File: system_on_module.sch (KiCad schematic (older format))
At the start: 1 part

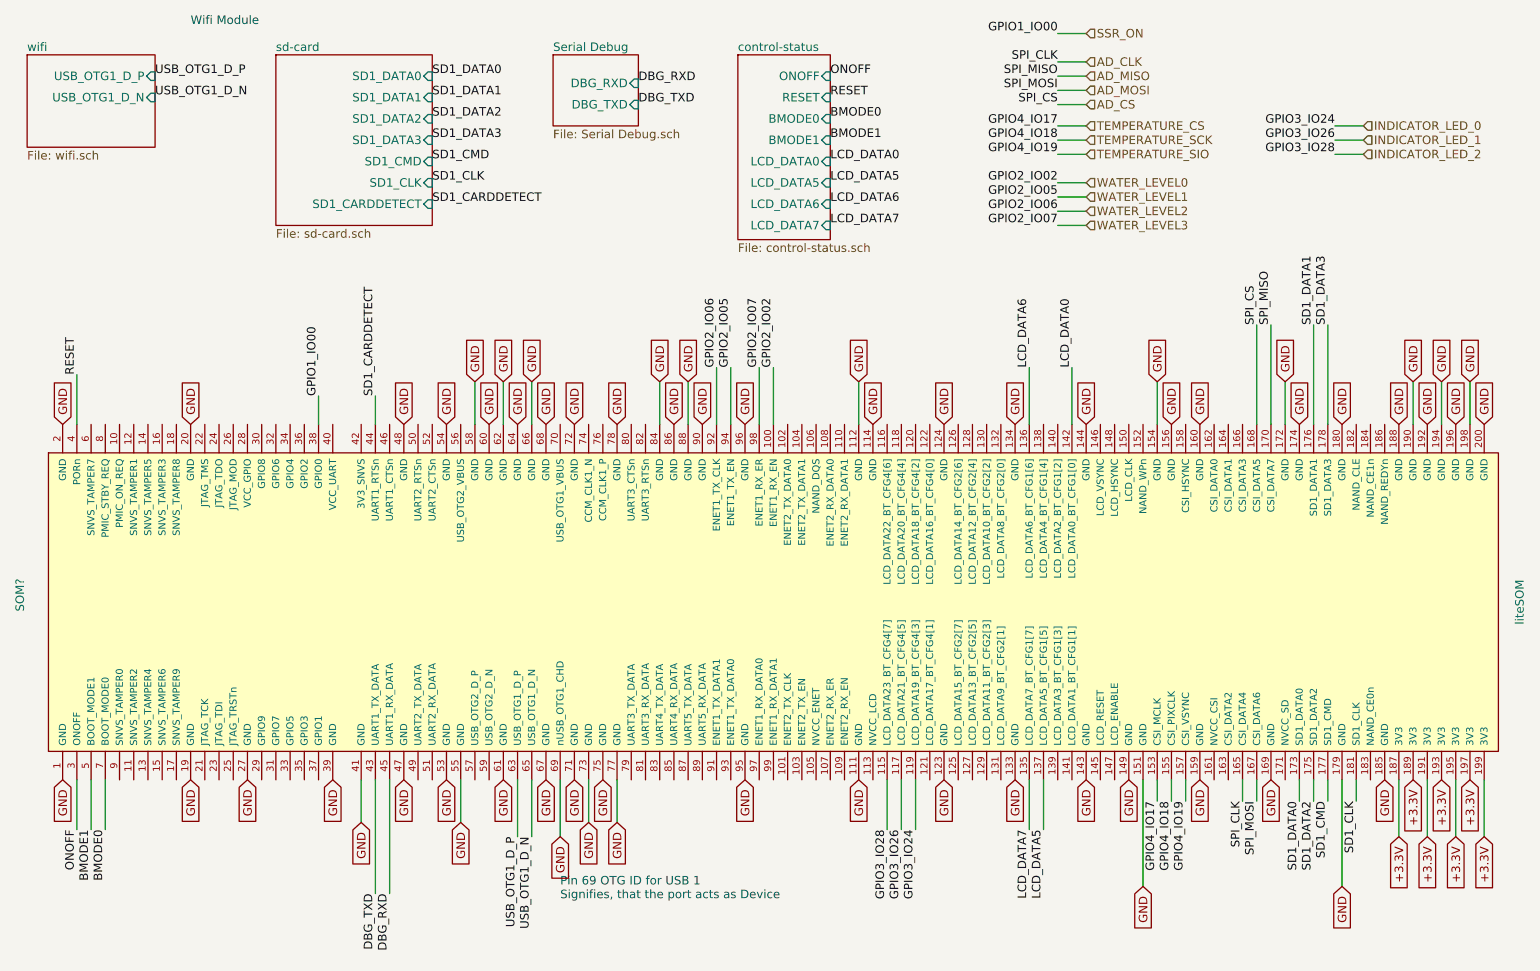
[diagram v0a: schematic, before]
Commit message: this version contains the datasheets and the footprints of the parts
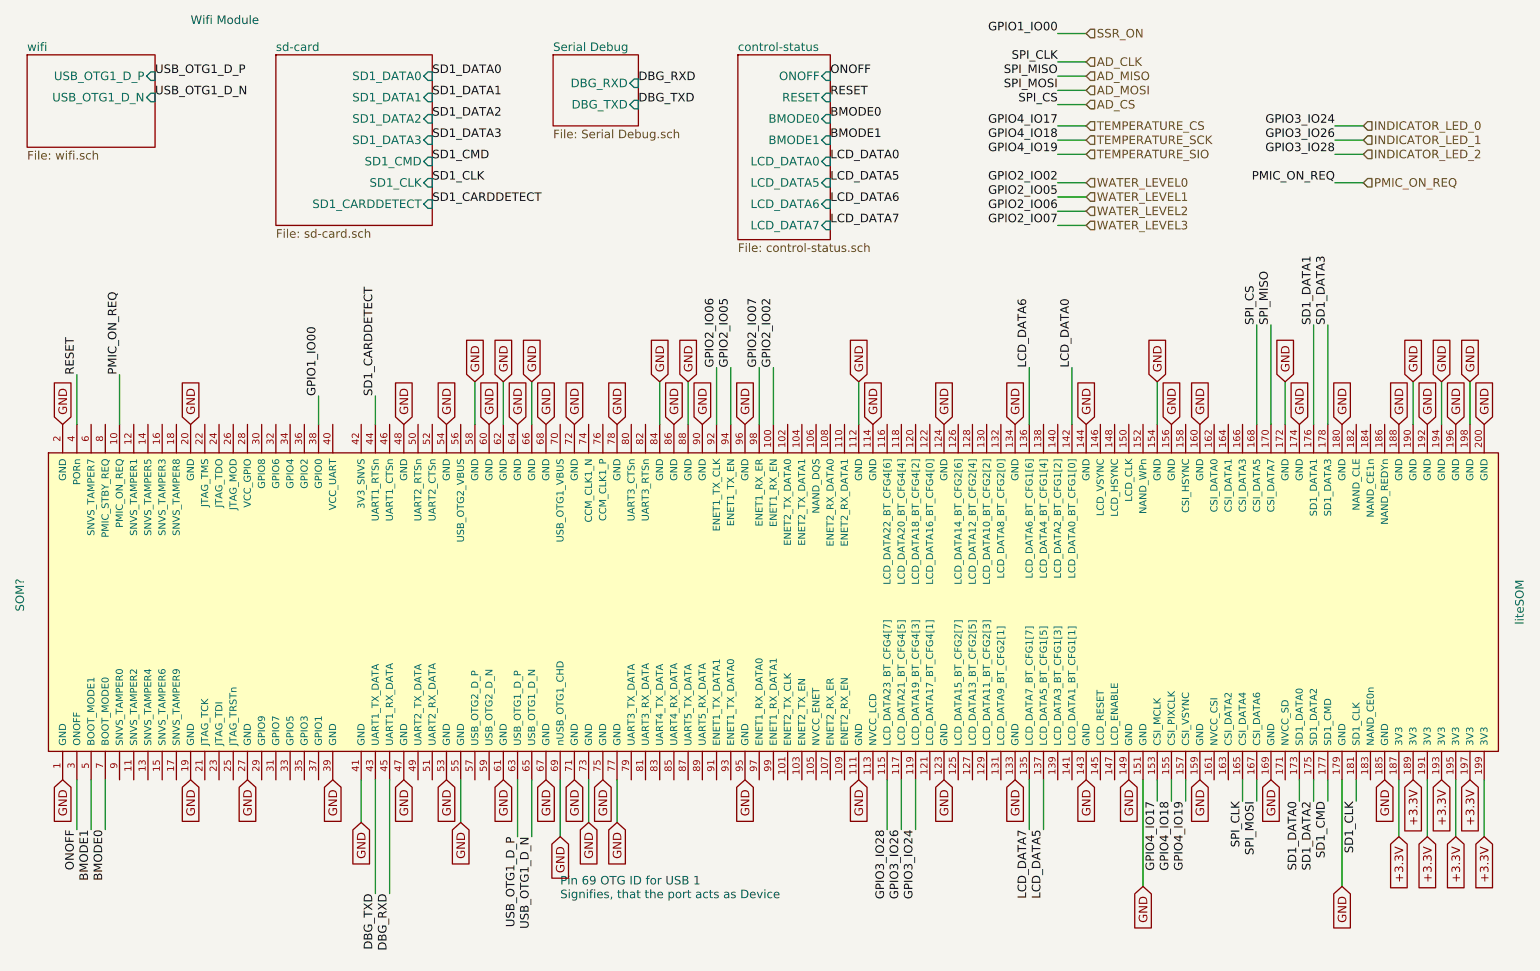
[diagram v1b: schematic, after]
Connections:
- net PMIC_ON_REQ: now reaches SOM?.10 (PMIC_ON_REQ)
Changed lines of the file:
@@
 Wire Wire Line
 	9900 6600 9900 5850
+Text Label 9850 1650 2    60   ~ 0
+PMIC_ON_REQ
+Text HLabel 10050 1650 2    60   Input ~ 0
+PMIC_ON_REQ
+Wire Wire Line
+	9850 1650 10050 1650
+Text Label 1300 3000 1    60   ~ 0
+PMIC_ON_REQ
+Wire Wire Line
+	1300 3000 1300 3350
 $EndSCHEMATC

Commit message: some issues fixed by the bugfixer; formal verification needed
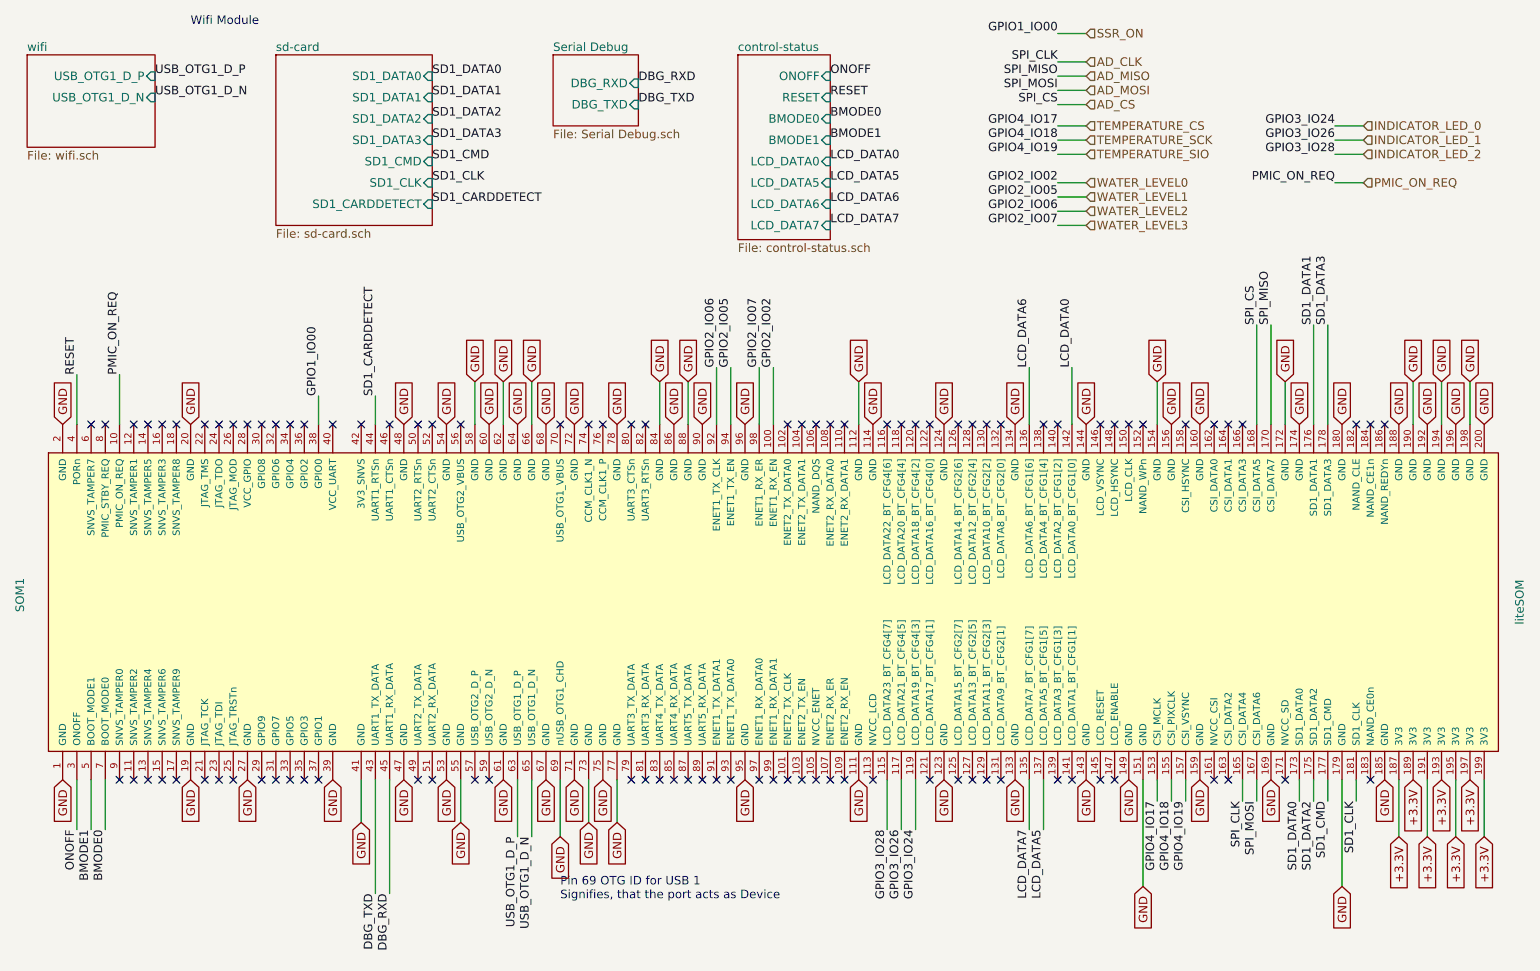
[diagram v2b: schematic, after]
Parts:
- gave numbers to parts that had none: 1
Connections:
- no-connect marks 0 -> 97
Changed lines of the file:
@@
 +3.3V
 $Comp
-L liteSOM SOM?
+L liteSOM SOM1
 U 1 1 599EACA1
 P 5900 3550
-F 0 "SOM?" V 600 2550 60  0000 C CNN
+F 0 "SOM1" V 600 2550 60  0000 C CNN
 F 1 "liteSOM" V 11150 2500 60  0000 C CNN
 F 2 "Sockets:Socket_SODIMM_DDR1-2_TE_1612618_Debug" H 5900 3550 60  0001 C CNN
@@
 Wire Wire Line
 	1300 3000 1300 3350
+NoConn ~ 7200 3350
+NoConn ~ 7300 3350
+NoConn ~ 7400 3350
+NoConn ~ 7500 3350
+NoConn ~ 7800 3350
+NoConn ~ 7900 3350
+NoConn ~ 8200 3350
+NoConn ~ 8300 3350
+NoConn ~ 8400 3350
+NoConn ~ 8500 3350
+NoConn ~ 8800 3350
+NoConn ~ 9000 3350
+NoConn ~ 9100 3350
+NoConn ~ 9200 3350
+NoConn ~ 10000 3350
+NoConn ~ 10100 3350
+NoConn ~ 10200 3350
+NoConn ~ 1100 3350
+NoConn ~ 1200 3350
+NoConn ~ 1400 3350
+NoConn ~ 1500 3350
+NoConn ~ 1600 3350
+NoConn ~ 1700 3350
+NoConn ~ 1900 3350
+NoConn ~ 2000 3350
+NoConn ~ 2100 3350
+NoConn ~ 2200 3350
+NoConn ~ 2300 3350
+NoConn ~ 2400 3350
+NoConn ~ 2500 3350
+NoConn ~ 2600 3350
+NoConn ~ 2800 3350
+NoConn ~ 3000 3350
+NoConn ~ 3200 3350
+NoConn ~ 3400 3350
+NoConn ~ 3500 3350
+NoConn ~ 3700 3350
+NoConn ~ 4600 3350
+NoConn ~ 4400 3350
+NoConn ~ 4700 3350
+NoConn ~ 4900 3350
+NoConn ~ 5000 3350
+NoConn ~ 6000 3350
+NoConn ~ 6100 3350
+NoConn ~ 6200 3350
+NoConn ~ 6300 3350
+NoConn ~ 6400 3350
+NoConn ~ 6700 3350
+NoConn ~ 6800 3350
+NoConn ~ 6900 3350
+NoConn ~ 7000 3350
+NoConn ~ 10100 5850
+NoConn ~ 9500 5850
+NoConn ~ 9100 5850
+NoConn ~ 9000 5850
+NoConn ~ 8300 5850
+NoConn ~ 8200 5850
+NoConn ~ 8000 5850
+NoConn ~ 7900 5850
+NoConn ~ 7500 5850
+NoConn ~ 7400 5850
+NoConn ~ 7300 5850
+NoConn ~ 7200 5850
+NoConn ~ 7000 5850
+NoConn ~ 4900 5850
+NoConn ~ 5000 5850
+NoConn ~ 5100 5850
+NoConn ~ 5200 5850
+NoConn ~ 5300 5850
+NoConn ~ 5400 5850
+NoConn ~ 5500 5850
+NoConn ~ 5600 5850
+NoConn ~ 5800 5850
+NoConn ~ 5900 5850
+NoConn ~ 6000 5850
+NoConn ~ 6100 5850
+NoConn ~ 6200 5850
+NoConn ~ 6300 5850
+NoConn ~ 6400 5850
+NoConn ~ 6600 5850
+NoConn ~ 1300 5850
+NoConn ~ 1400 5850
+NoConn ~ 1500 5850
+NoConn ~ 1600 5850
+NoConn ~ 1700 5850
+NoConn ~ 1900 5850
+NoConn ~ 2000 5850
+NoConn ~ 2100 5850
+NoConn ~ 2300 5850
+NoConn ~ 2400 5850
+NoConn ~ 2500 5850
+NoConn ~ 2600 5850
+NoConn ~ 2700 5850
+NoConn ~ 3400 5850
+NoConn ~ 3500 5850
+NoConn ~ 3800 5850
+NoConn ~ 3900 5850
 $EndSCHEMATC

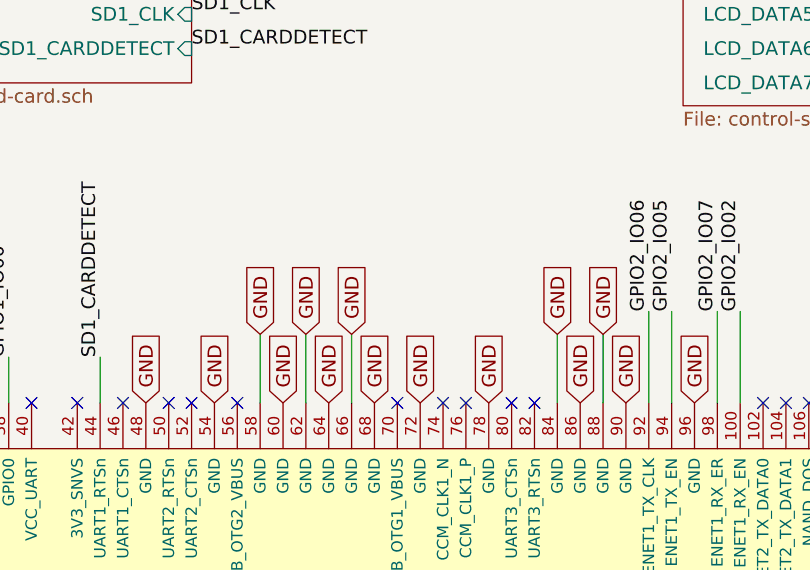
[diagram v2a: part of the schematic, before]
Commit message: I have verified the so-dimm, and added 5V with an 1ohm resistor to drive the usb pins.
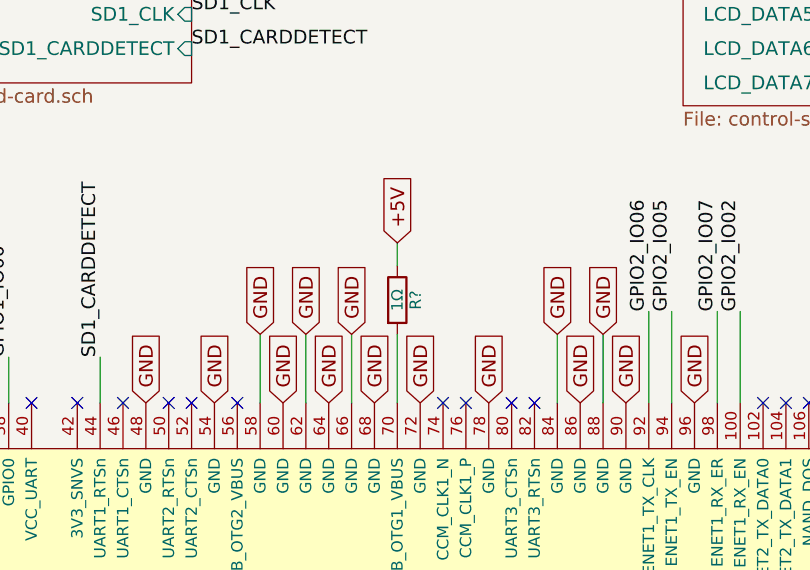
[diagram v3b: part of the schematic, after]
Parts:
- added R?: 1Ω, Resistors_SMD:R_0603_HandSoldering, symbol R
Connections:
- net at SOM1.70 (USB_OTG1_VBUS): now also R?.2
- new net +5V: R?.1
- no-connect marks 97 -> 96
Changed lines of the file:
@@
 NoConn ~ 3700 3350
 NoConn ~ 4600 3350
-NoConn ~ 4400 3350
 NoConn ~ 4700 3350
 NoConn ~ 4900 3350
@@
 NoConn ~ 3800 5850
 NoConn ~ 3900 5850
+Text GLabel 4400 2650 1    60   Input ~ 0
++5V
+$Comp
+L R R?
+U 1 1 59AB3248
+P 4400 2900
+F 0 "R?" V 4480 2900 50  0000 C CNN
+F 1 "1Ω" V 4400 2900 50  0000 C CNN
+F 2 "Resistors_SMD:R_0603_HandSoldering" V 4330 2900 50  0001 C CNN
+F 3 "http://hu.farnell.com/multicomp/mcwr06w1r00ftl/res-thick-film-1r-1-0-1w-0603/dp/2447289" H 4400 2900 50  0001 C CNN
+	1    4400 2900
+	1    0    0    -1
+$EndComp
+Wire Wire Line
+	4400 3350 4400 3050
+Wire Wire Line
+	4400 2750 4400 2650
 $EndSCHEMATC

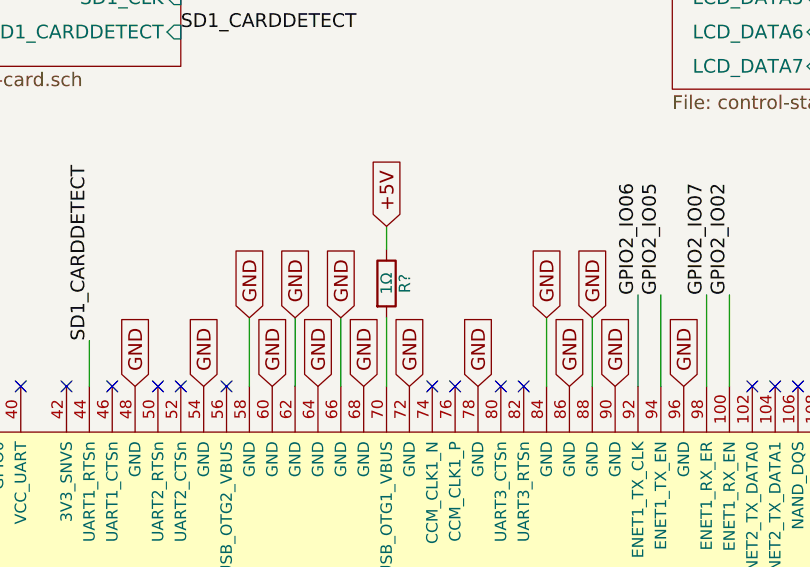
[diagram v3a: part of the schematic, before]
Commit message: part numbers generated;
pcb generation started
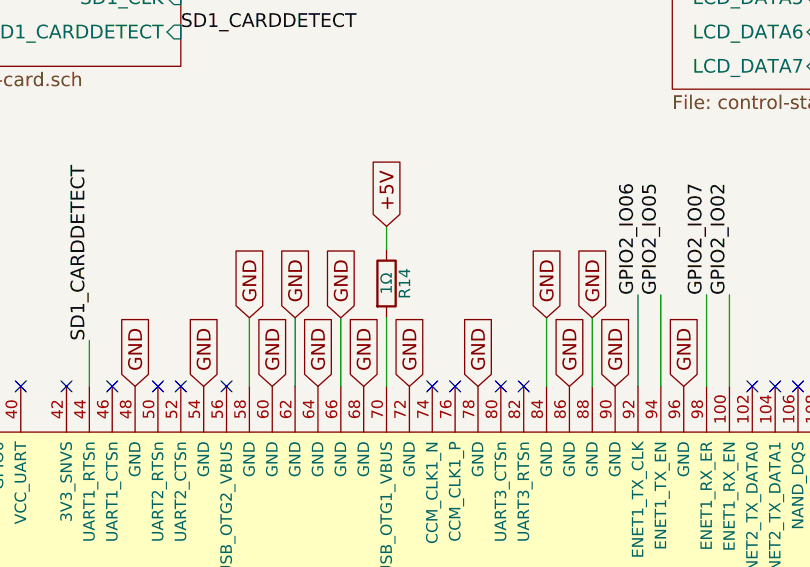
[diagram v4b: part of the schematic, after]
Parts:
- gave numbers to parts that had none: 1
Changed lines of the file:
@@
 +5V
 $Comp
-L R R?
+L R R14
 U 1 1 59AB3248
 P 4400 2900
-F 0 "R?" V 4480 2900 50  0000 C CNN
+F 0 "R14" V 4480 2900 50  0000 C CNN
 F 1 "1Ω" V 4400 2900 50  0000 C CNN
 F 2 "Resistors_SMD:R_0603_HandSoldering" V 4330 2900 50  0001 C CNN

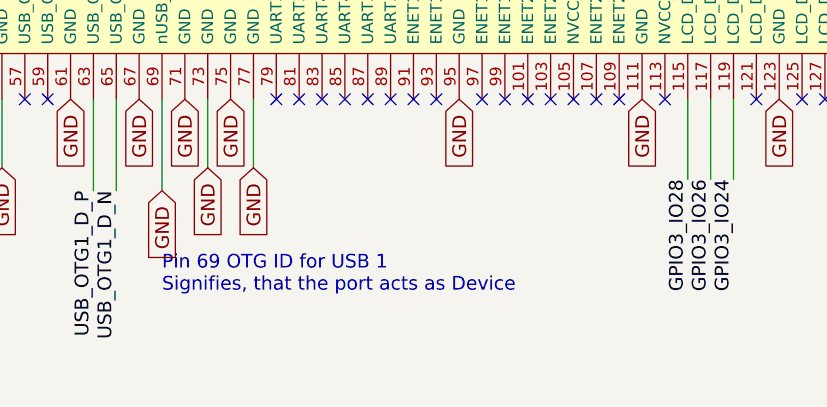
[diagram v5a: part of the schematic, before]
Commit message: This version contains the final revision before the part footprint verification.
- The fuse is now moved outside of the power module before any parts
- The wifi module has an additional pair of 22R differential resistors
- The minor moves in the power power supply of the wifi module
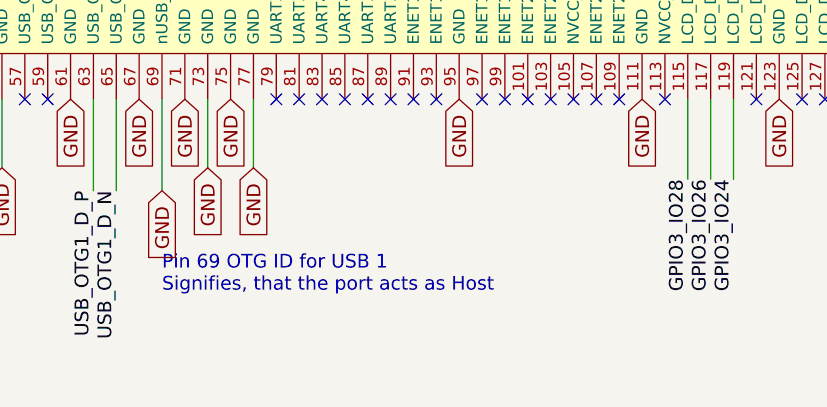
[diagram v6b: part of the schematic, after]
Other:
- note added: "Pin 69 OTG ID for USB 1 \nSignifies, that the port acts as Host"
- note removed: "Pin 69 OTG ID for USB 1 \nSignifies, that the port acts as Device"
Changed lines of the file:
@@
 GND
 Text Notes 4400 6700 0    60   ~ 0
-Pin 69 OTG ID for USB 1 \nSignifies, that the port acts as Device
+Pin 69 OTG ID for USB 1 \nSignifies, that the port acts as Host
 Wire Wire Line
 	4600 6150 4600 5850

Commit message: I have corrected the footprints of the parts which have arrived
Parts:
- SOM1: footprint Sockets:Socket_SODIMM_DDR1-2_TE_1612618_Debug -> water:Socket_SODIMM_DDR1-Farnell_2396418_Debug
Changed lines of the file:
@@
 F 0 "SOM1" V 600 2550 60  0000 C CNN
 F 1 "liteSOM" V 11150 2500 60  0000 C CNN
-F 2 "Sockets:Socket_SODIMM_DDR1-2_TE_1612618_Debug" H 5900 3550 60  0001 C CNN
-F 3 "" H 5900 3550 60  0001 C CNN
+F 2 "water:Socket_SODIMM_DDR1-Farnell_2396418_Debug" H 5900 3550 60  0001 C CNN
+F 3 "http://hu.farnell.com/te-connectivity-amp/1612618-4/connector-dimm-socket-200pos/dp/2396418" H 5900 3550 60  0001 C CNN
 	1    5900 3550
 	1    0    0    -1

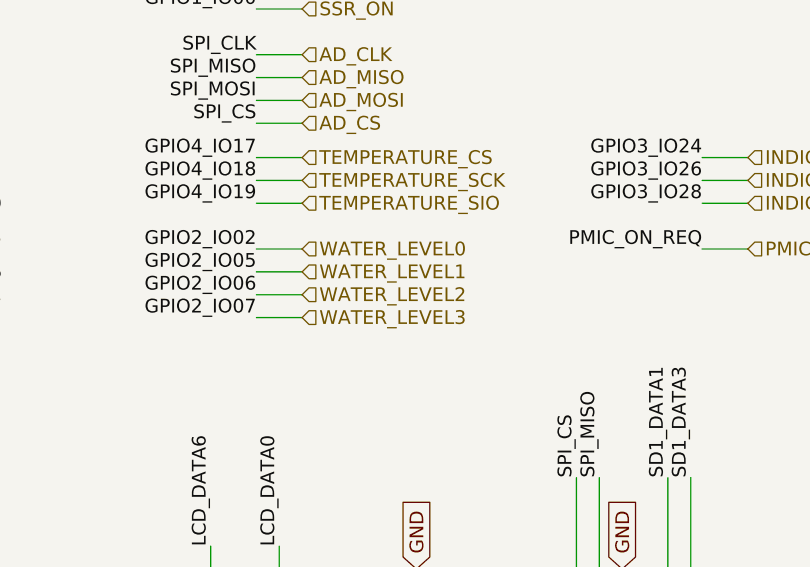
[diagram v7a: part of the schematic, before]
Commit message: I have re-routed the table after the footprints of the parts have been verified.
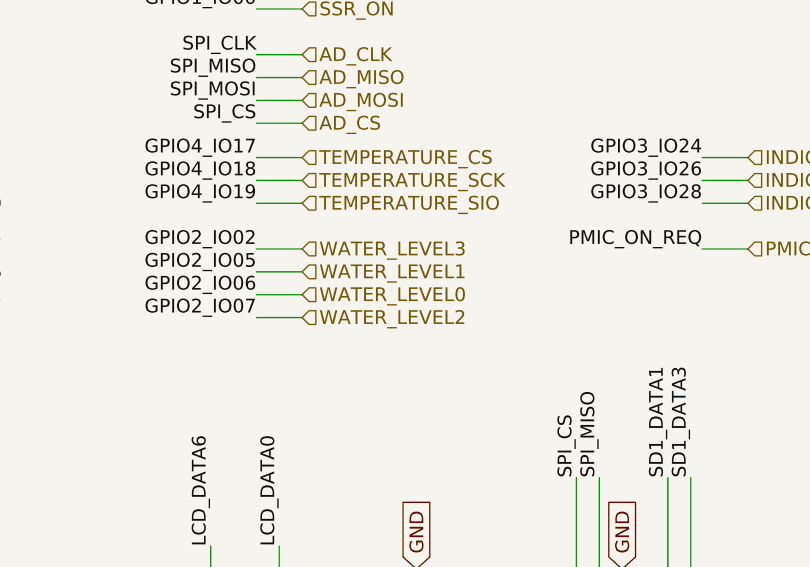
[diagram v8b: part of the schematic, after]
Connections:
- net WATER_LEVEL0: now also SOM1.92 (ENET1_TX_CLK); no longer SOM1.100 (ENET1_RX_EN)
- net WATER_LEVEL2: now also SOM1.98 (ENET1_RX_ER); no longer SOM1.92 (ENET1_TX_CLK)
- net WATER_LEVEL3: now also SOM1.100 (ENET1_RX_EN); no longer SOM1.98 (ENET1_RX_ER)
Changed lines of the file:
@@
 Text HLabel 8100 1450 2    60   Input ~ 0
 TEMPERATURE_SIO
-Text HLabel 8100 1650 2    60   Input ~ 0
+Text HLabel 8100 1850 2    60   Input ~ 0
 WATER_LEVEL0
 Text HLabel 8100 1750 2    60   Input ~ 0
 WATER_LEVEL1
-Text HLabel 8100 1850 2    60   Input ~ 0
+Text HLabel 8100 1950 2    60   Input ~ 0
 WATER_LEVEL2
-Text HLabel 8100 1950 2    60   Input ~ 0
+Text HLabel 8100 1650 2    60   Input ~ 0
 WATER_LEVEL3
 Text HLabel 10050 1250 2    60   Input ~ 0
